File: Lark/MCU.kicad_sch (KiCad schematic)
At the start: 19 parts, among them J9 0530470410, U14 STM32H743VIT6, Y1 8Mhz

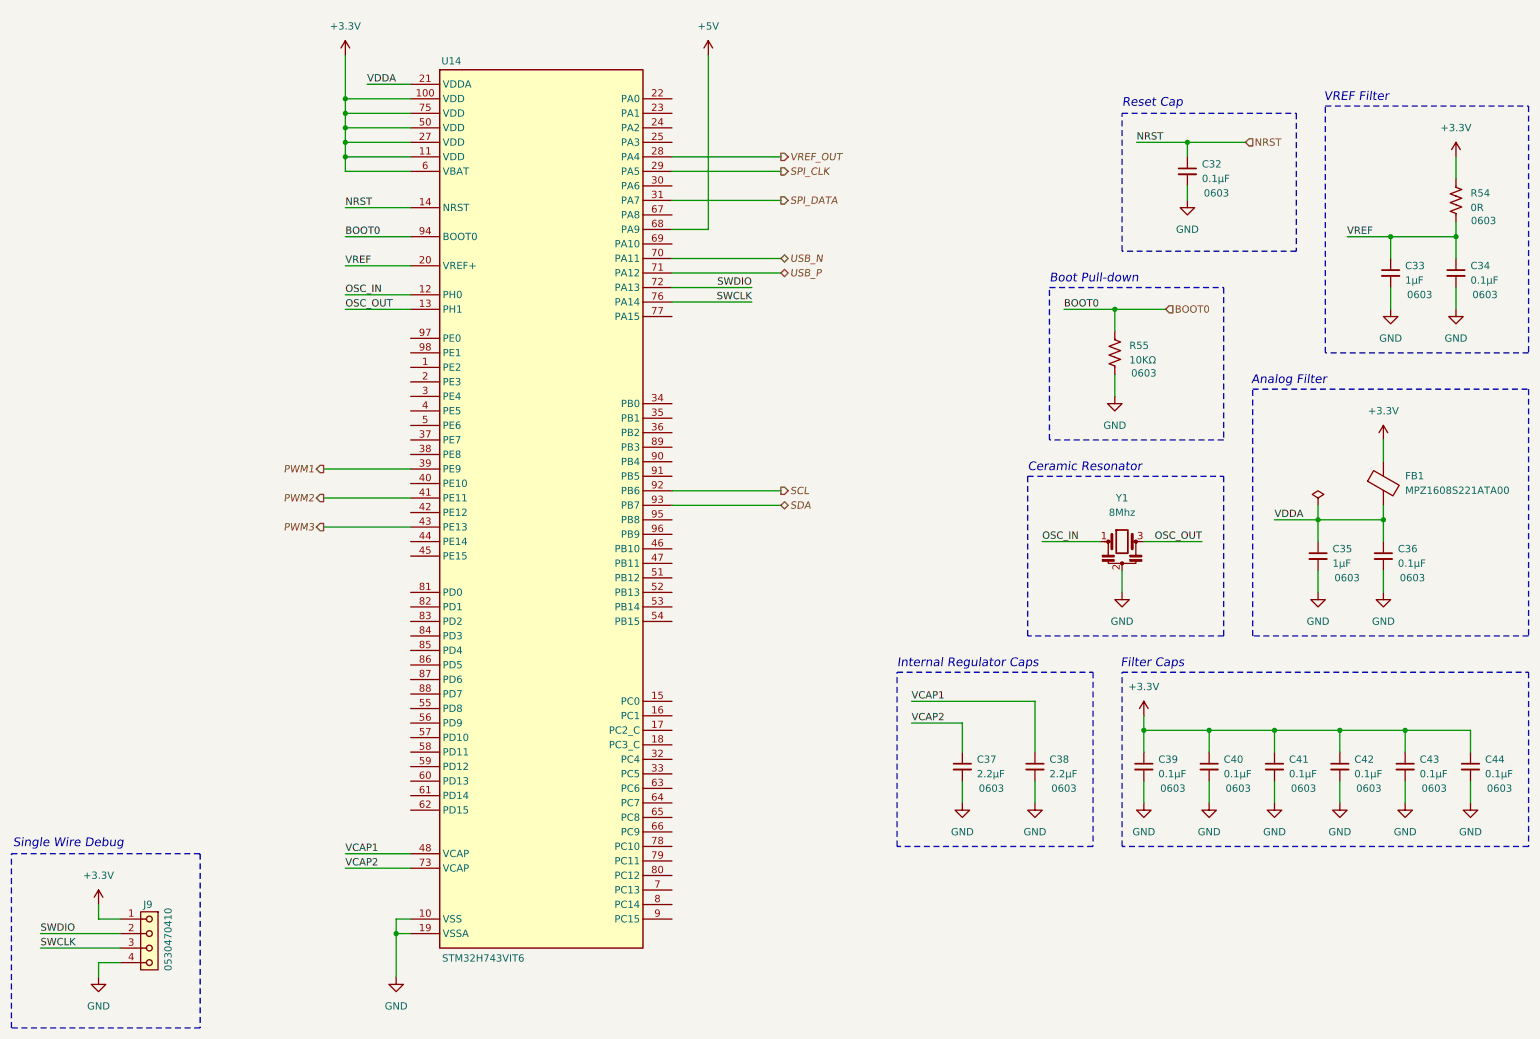
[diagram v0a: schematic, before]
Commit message: Updated schematic, WIP
- Added NOR flash part.
- Added new CubeMX config file.
- Reannotated the schematic.
- Made some more connections to the MCU.
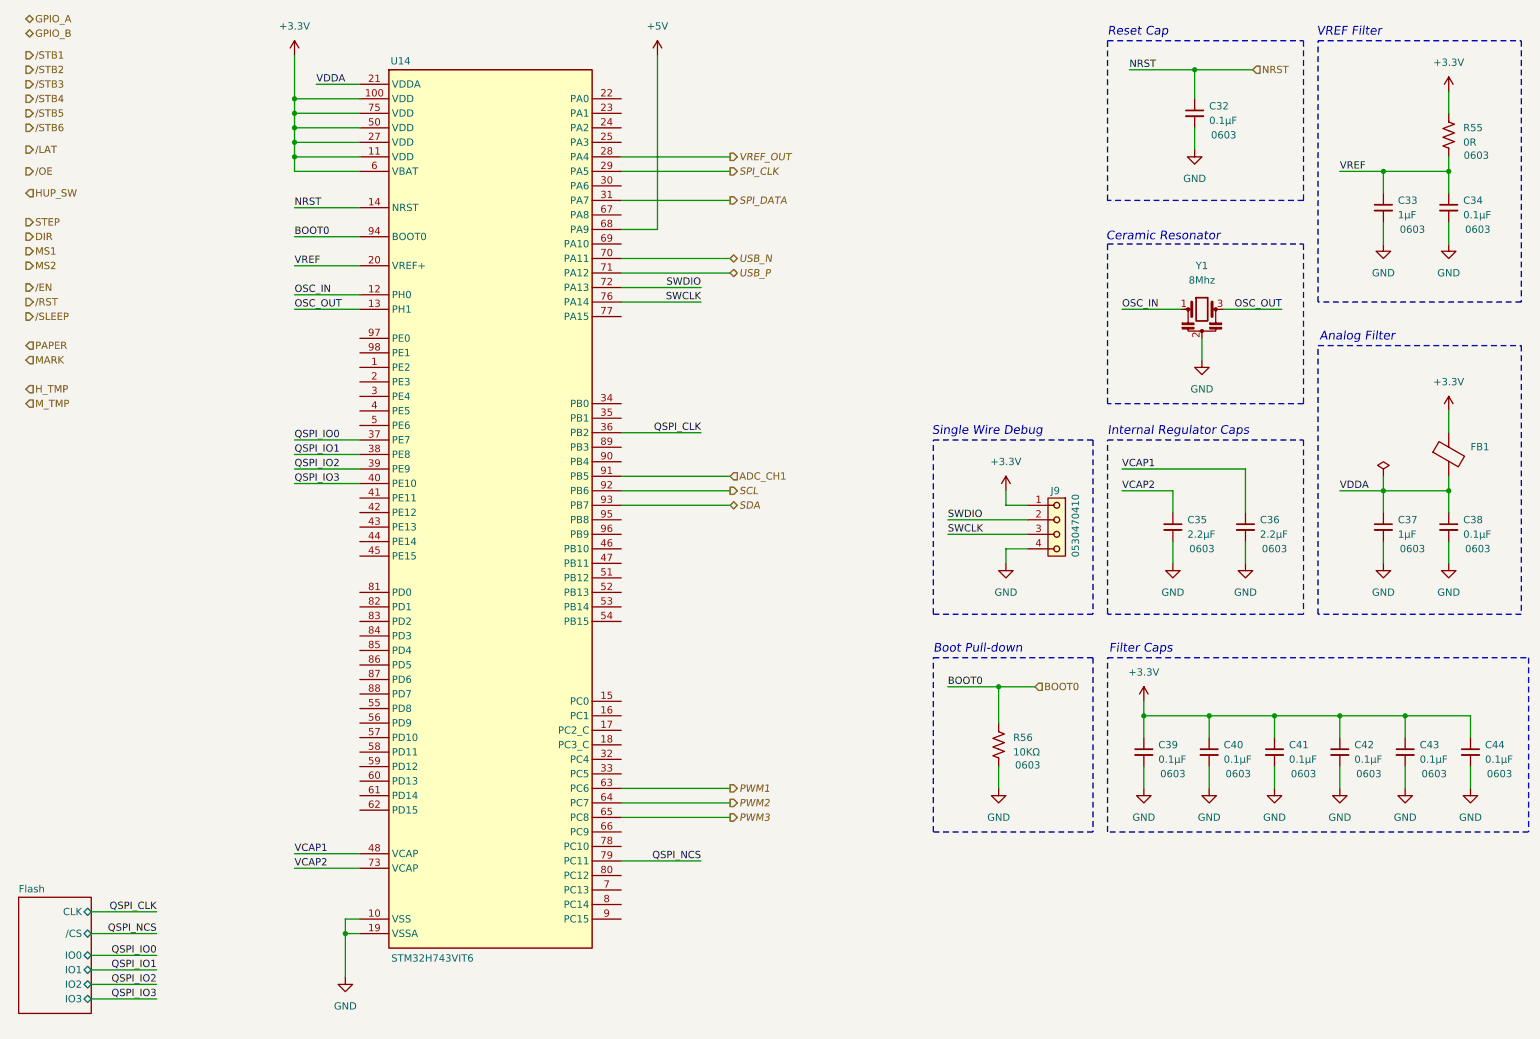
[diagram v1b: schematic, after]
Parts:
- FB1: value MPZ1608S221ATA00 -> 220 Ohms
- renumbered C37 to C35, C38 to C36, C35 to C37, C36 to C38, R54 to R55, R55 to R56
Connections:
- net PWM1: now also U14.63 (PC6); no longer U14.39 (PE9)
- net PWM2: now also U14.64 (PC7); no longer U14.41 (PE11)
- net PWM3: now also U14.65 (PC8); no longer U14.43 (PE13)
- net QSPI_CLK: now reaches U14.36 (PB2)
- net QSPI_IO0: now reaches U14.37 (PE7)
- net QSPI_IO1: now reaches U14.38 (PE8)
- net QSPI_IO3: now reaches U14.40 (PE10)
- net QSPI_NCS: now reaches U14.79 (PC11)
- net ADC_CH1: now reaches U14.91 (PB5)
- new net QSPI_IO2: U14.39 (PE9)
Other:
- added sheet Flash (Flash.kicad_sch)
- moved on the sheet: C32, C33, C34, C35, C36, C37, C38, C39, C40, C41, C42, C43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

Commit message: Update, WIP
- Added TVS diode to 24v Supply.
- Fixed bleeder circuit at some point (I think it was this commit)
- Added Jumper to connect NTC to ADC. (again I think it was this commit)
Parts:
- renumbered R55 to R58, R56 to R59
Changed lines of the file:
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@@
 		(dnp no)
 		(fields_autoplaced yes)
-		(property "Reference" "#PWR0166"
+		(property "Reference" "#PWR0170"
 			(at 219.71 119.38 0)
 			(effects
@@
 			(project "Lark"
 				(path "/a351af57-4353-47da-9f45-7393de572768/510bbd44-ee11-40bc-952d-6cd0def4c817"
-					(reference "#PWR0166")
+					(reference "#PWR0170")
 					(unit 1)
 				)
@@
 		(dnp no)
 		(fields_autoplaced yes)
-		(property "Reference" "#PWR0159"
+		(property "Reference" "#PWR0163"
 			(at 223.52 46.99 0)
 			(effects
@@
 			(project "Lark"
 				(path "/a351af57-4353-47da-9f45-7393de572768/510bbd44-ee11-40bc-952d-6cd0def4c817"
-					(reference "#PWR0159")
+					(reference "#PWR0163")
 					(unit 1)
 				)
@@
 		(dnp no)
 		(fields_autoplaced yes)
-		(property "Reference" "#PWR0175"
+		(property "Reference" "#PWR0179"
 			(at 248.92 158.75 0)
 			(effects
@@
 			(project "Lark"
 				(path "/a351af57-4353-47da-9f45-7393de572768/510bbd44-ee11-40bc-952d-6cd0def4c817"
-					(reference "#PWR0175")
+					(reference "#PWR0179")
 					(unit 1)
 				)
@@
 		(dnp no)
 		(fields_autoplaced yes)
-		(property "Reference" "#PWR0160"
+		(property "Reference" "#PWR0164"
 			(at 256.54 63.5 0)
 			(effects
@@
 			(project "Lark"
 				(path "/a351af57-4353-47da-9f45-7393de572768/510bbd44-ee11-40bc-952d-6cd0def4c817"
-					(reference "#PWR0160")
+					(reference "#PWR0164")
 					(unit 1)
 				)
@@
 		(on_board yes)
 		(dnp no)
-		(property "Reference" "R56"
+		(property "Reference" "R59"
 			(at 191.77 143.5099 0)
 			(effects
@@
 			(project "Lark"
 				(path "/a351af57-4353-47da-9f45-7393de572768/510bbd44-ee11-40bc-952d-6cd0def4c817"
-					(reference "R56")
+					(reference "R59")
 					(unit 1)
 				)
@@
 		(dnp no)
 		(fields_autoplaced yes)
-		(property "Reference" "#PWR0173"
+		(property "Reference" "#PWR0177"
 			(at 226.06 158.75 0)
 			(effects
@@
 			(project "Lark"
 				(path "/a351af57-4353-47da-9f45-7393de572768/510bbd44-ee11-40bc-952d-6cd0def4c817"
-					(reference "#PWR0173")
+					(reference "#PWR0177")
 					(unit 1)
 				)
@@
 		(dnp no)
 		(fields_autoplaced yes)
-		(property "Reference" "#PWR0165"
+		(property "Reference" "#PWR0169"
 			(at 190.5 119.38 0)
 			(effects
@@
 			(project "Lark"
 				(path "/a351af57-4353-47da-9f45-7393de572768/510bbd44-ee11-40bc-952d-6cd0def4c817"
-					(reference "#PWR0165")
+					(reference "#PWR0169")
 					(unit 1)
 				)
@@
 		(dnp no)
 		(fields_autoplaced yes)
-		(property "Reference" "#PWR0168"
+		(property "Reference" "#PWR0172"
 			(at 256.54 119.38 0)
 			(effects
@@
 			(project "Lark"
 				(path "/a351af57-4353-47da-9f45-7393de572768/510bbd44-ee11-40bc-952d-6cd0def4c817"
-					(reference "#PWR0168")
+					(reference "#PWR0172")
 					(unit 1)
 				)
@@
 		(dnp no)
 		(fields_autoplaced yes)
-		(property "Reference" "#PWR0176"
+		(property "Reference" "#PWR0180"
 			(at 260.35 158.75 0)
 			(effects
@@
 			(project "Lark"
 				(path "/a351af57-4353-47da-9f45-7393de572768/510bbd44-ee11-40bc-952d-6cd0def4c817"
-					(reference "#PWR0176")
+					(reference "#PWR0180")
 					(unit 1)
 				)
@@
 		(dnp no)
 		(fields_autoplaced yes)
-		(property "Reference" "#PWR0167"
+		(property "Reference" "#PWR0171"
 			(at 232.41 119.38 0)
 			(effects
@@
 			(project "Lark"
 				(path "/a351af57-4353-47da-9f45-7393de572768/510bbd44-ee11-40bc-952d-6cd0def4c817"
-					(reference "#PWR0167")
+					(reference "#PWR0171")
 					(unit 1)
 				)
@@
 		(dnp no)
 		(fields_autoplaced yes)
-		(property "Reference" "#PWR0163"
+		(property "Reference" "#PWR0167"
 			(at 267.97 90.17 0)
 			(effects
@@
 			(project "Lark"
 				(path "/a351af57-4353-47da-9f45-7393de572768/510bbd44-ee11-40bc-952d-6cd0def4c817"
-					(reference "#PWR0163")
+					(reference "#PWR0167")
 					(unit 1)
 				)
@@
 		(dnp no)
 		(fields_autoplaced yes)
-		(property "Reference" "#PWR0164"
+		(property "Reference" "#PWR0168"
 			(at 190.5 104.14 0)
 			(effects
@@
 			(project "Lark"
 				(path "/a351af57-4353-47da-9f45-7393de572768/510bbd44-ee11-40bc-952d-6cd0def4c817"
-					(reference "#PWR0164")
+					(reference "#PWR0168")
 					(unit 1)
 				)
@@
 		(dnp no)
 		(fields_autoplaced yes)
-		(property "Reference" "#PWR0177"
+		(property "Reference" "#PWR0181"
 			(at 271.78 158.75 0)
 			(effects
@@
 			(project "Lark"
 				(path "/a351af57-4353-47da-9f45-7393de572768/510bbd44-ee11-40bc-952d-6cd0def4c817"
-					(reference "#PWR0177")
+					(reference "#PWR0181")
 					(unit 1)
 				)
@@
 		(dnp no)
 		(fields_autoplaced yes)
-		(property "Reference" "#PWR0157"
+		(property "Reference" "#PWR0161"
 			(at 129.54 27.94 0)
 			(effects
@@
 			(project "Lark"
 				(path "/a351af57-4353-47da-9f45-7393de572768/510bbd44-ee11-40bc-952d-6cd0def4c817"
-					(reference "#PWR0157")
+					(reference "#PWR0161")
 					(unit 1)
 				)
@@
 		(dnp no)
 		(fields_autoplaced yes)
-		(property "Reference" "#PWR0161"
+		(property "Reference" "#PWR0165"
 			(at 267.97 63.5 0)
 			(effects
@@
 			(project "Lark"
 				(path "/a351af57-4353-47da-9f45-7393de572768/510bbd44-ee11-40bc-952d-6cd0def4c817"
-					(reference "#PWR0161")
+					(reference "#PWR0165")
 					(unit 1)
 				)
@@
 		(dnp no)
 		(fields_autoplaced yes)
-		(property "Reference" "#PWR0156"
+		(property "Reference" "#PWR0160"
 			(at 66.04 27.94 0)
 			(effects
@@
 			(project "Lark"
 				(path "/a351af57-4353-47da-9f45-7393de572768/510bbd44-ee11-40bc-952d-6cd0def4c817"
-					(reference "#PWR0156")
+					(reference "#PWR0160")
 					(unit 1)
 				)
@@
 		(dnp no)
 		(fields_autoplaced yes)
-		(property "Reference" "#PWR0158"
+		(property "Reference" "#PWR0162"
 			(at 267.97 34.29 0)
 			(effects
@@
 			(project "Lark"
 				(path "/a351af57-4353-47da-9f45-7393de572768/510bbd44-ee11-40bc-952d-6cd0def4c817"
-					(reference "#PWR0158")
+					(reference "#PWR0162")
 					(unit 1)
 				)
@@
 		(dnp no)
 		(fields_autoplaced yes)
-		(property "Reference" "#PWR0169"
+		(property "Reference" "#PWR0173"
 			(at 267.97 119.38 0)
 			(effects
@@
 			(project "Lark"
 				(path "/a351af57-4353-47da-9f45-7393de572768/510bbd44-ee11-40bc-952d-6cd0def4c817"
-					(reference "#PWR0169")
+					(reference "#PWR0173")
 					(unit 1)
 				)
@@
 		(dnp no)
 		(fields_autoplaced yes)
-		(property "Reference" "#PWR0172"
+		(property "Reference" "#PWR0176"
 			(at 214.63 158.75 0)
 			(effects
@@
 			(project "Lark"
 				(path "/a351af57-4353-47da-9f45-7393de572768/510bbd44-ee11-40bc-952d-6cd0def4c817"
-					(reference "#PWR0172")
+					(reference "#PWR0176")
 					(unit 1)
 				)
@@
 		(on_board yes)
 		(dnp no)
-		(property "Reference" "R55"
+		(property "Reference" "R58"
 			(at 270.51 36.8299 0)
 			(effects
@@
 			(project "Lark"
 				(path "/a351af57-4353-47da-9f45-7393de572768/510bbd44-ee11-40bc-952d-6cd0def4c817"
-					(reference "R55")
+					(reference "R58")
 					(unit 1)
 				)
@@
 		(dnp no)
 		(fields_autoplaced yes)
-		(property "Reference" "#PWR0174"
+		(property "Reference" "#PWR0178"
 			(at 237.49 158.75 0)
 			(effects
@@
 			(project "Lark"
 				(path "/a351af57-4353-47da-9f45-7393de572768/510bbd44-ee11-40bc-952d-6cd0def4c817"
-					(reference "#PWR0174")
+					(reference "#PWR0178")
 					(unit 1)
 				)
@@
 		(dnp no)
 		(fields_autoplaced yes)
-		(property "Reference" "#PWR0162"
+		(property "Reference" "#PWR0166"
 			(at 224.79 83.82 0)
 			(effects
@@
 			(project "Lark"
 				(path "/a351af57-4353-47da-9f45-7393de572768/510bbd44-ee11-40bc-952d-6cd0def4c817"
-					(reference "#PWR0162")
+					(reference "#PWR0166")
 					(unit 1)
 				)
@@
 		(dnp no)
 		(fields_autoplaced yes)
-		(property "Reference" "#PWR0178"
+		(property "Reference" "#PWR0182"
 			(at 74.93 191.77 0)
 			(effects
@@
 			(project "Lark"
 				(path "/a351af57-4353-47da-9f45-7393de572768/510bbd44-ee11-40bc-952d-6cd0def4c817"
-					(reference "#PWR0178")
+					(reference "#PWR0182")
 					(unit 1)
 				)
@@
 		(dnp no)
 		(fields_autoplaced yes)
-		(property "Reference" "#PWR0171"
+		(property "Reference" "#PWR0175"
 			(at 189.23 158.75 0)
 			(effects
@@
 			(project "Lark"
 				(path "/a351af57-4353-47da-9f45-7393de572768/510bbd44-ee11-40bc-952d-6cd0def4c817"
-					(reference "#PWR0171")
+					(reference "#PWR0175")
 					(unit 1)
 				)
@@
 		(dnp no)
 		(fields_autoplaced yes)
-		(property "Reference" "#PWR0170"
+		(property "Reference" "#PWR0174"
 			(at 214.63 140.97 0)
 			(effects
@@
 			(project "Lark"
 				(path "/a351af57-4353-47da-9f45-7393de572768/510bbd44-ee11-40bc-952d-6cd0def4c817"
-					(reference "#PWR0170")
+					(reference "#PWR0174")
 					(unit 1)
 				)
